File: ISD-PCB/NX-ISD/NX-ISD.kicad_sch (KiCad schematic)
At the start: 1 part

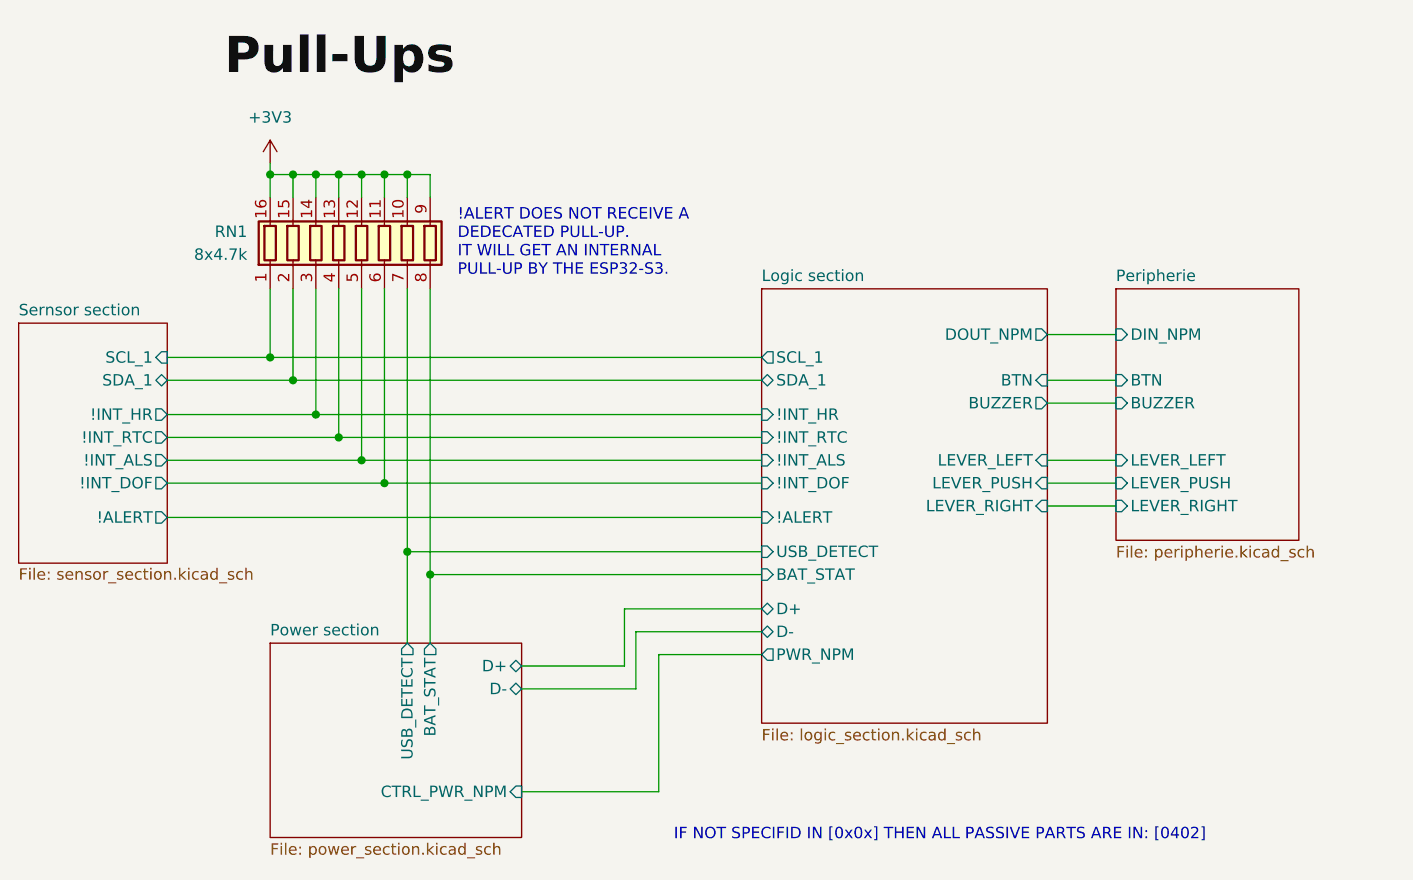
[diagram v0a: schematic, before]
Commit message: Fixed: polarity of NPM Pmos
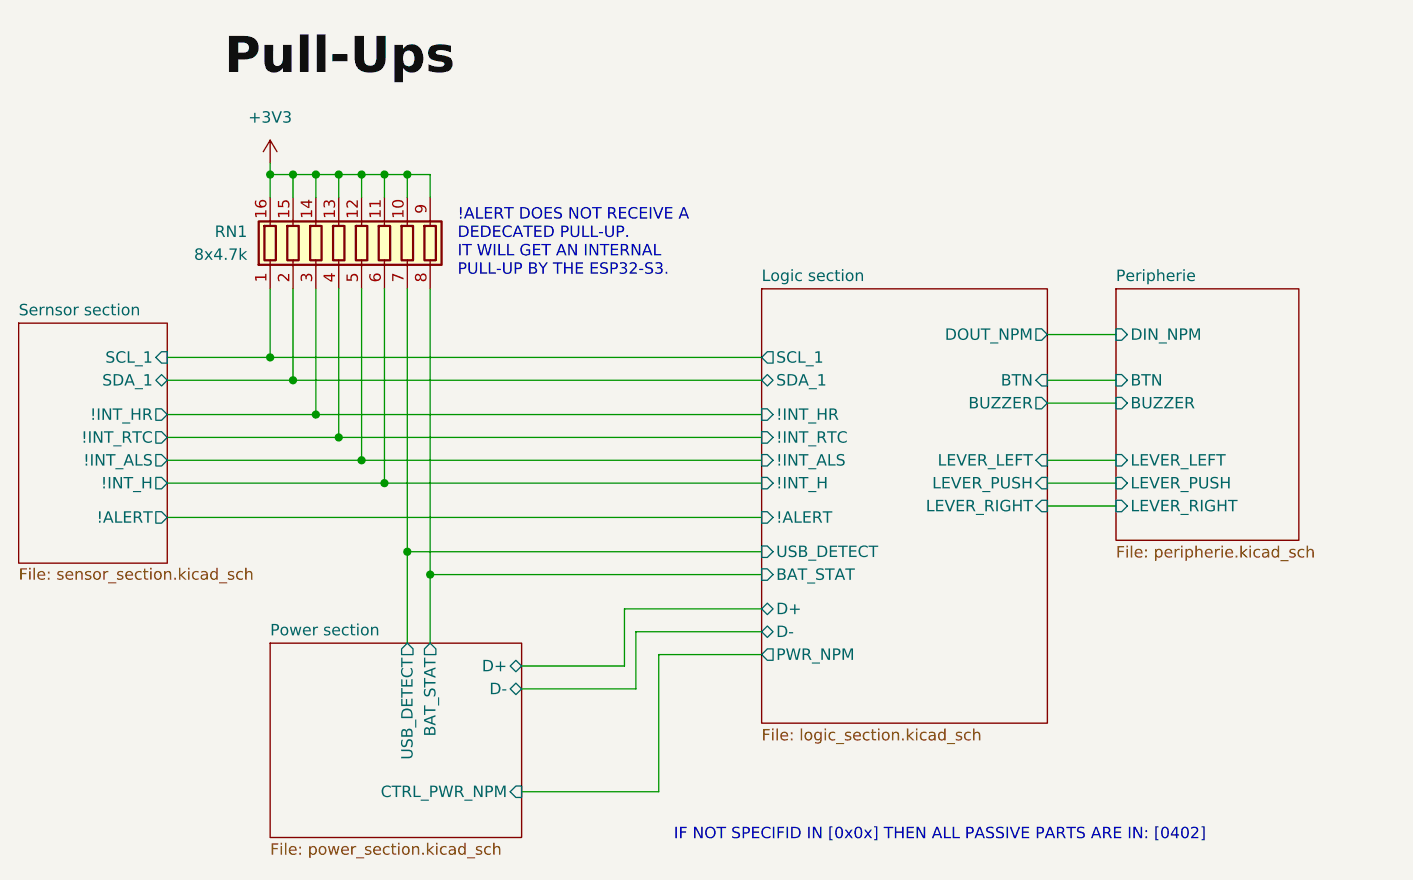
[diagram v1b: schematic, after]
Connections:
- net Logic section/!INT_DOF renamed Logic section/!INT_H
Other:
- sheet Logic section ports: added !INT_H; removed !INT_DOF
- sheet Sernsor section ports: added !INT_H; removed !INT_DOF
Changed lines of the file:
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@@
 			)
 		)
-		(pin "!INT_DOF" input
+		(pin "!INT_H" input
 			(at 104.14 67.31 180)
 			(effects
@@
 			)
 		)
-		(pin "!INT_DOF" output
+		(pin "!INT_H" output
 			(at 38.1 67.31 0)
 			(effects

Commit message: updated labels
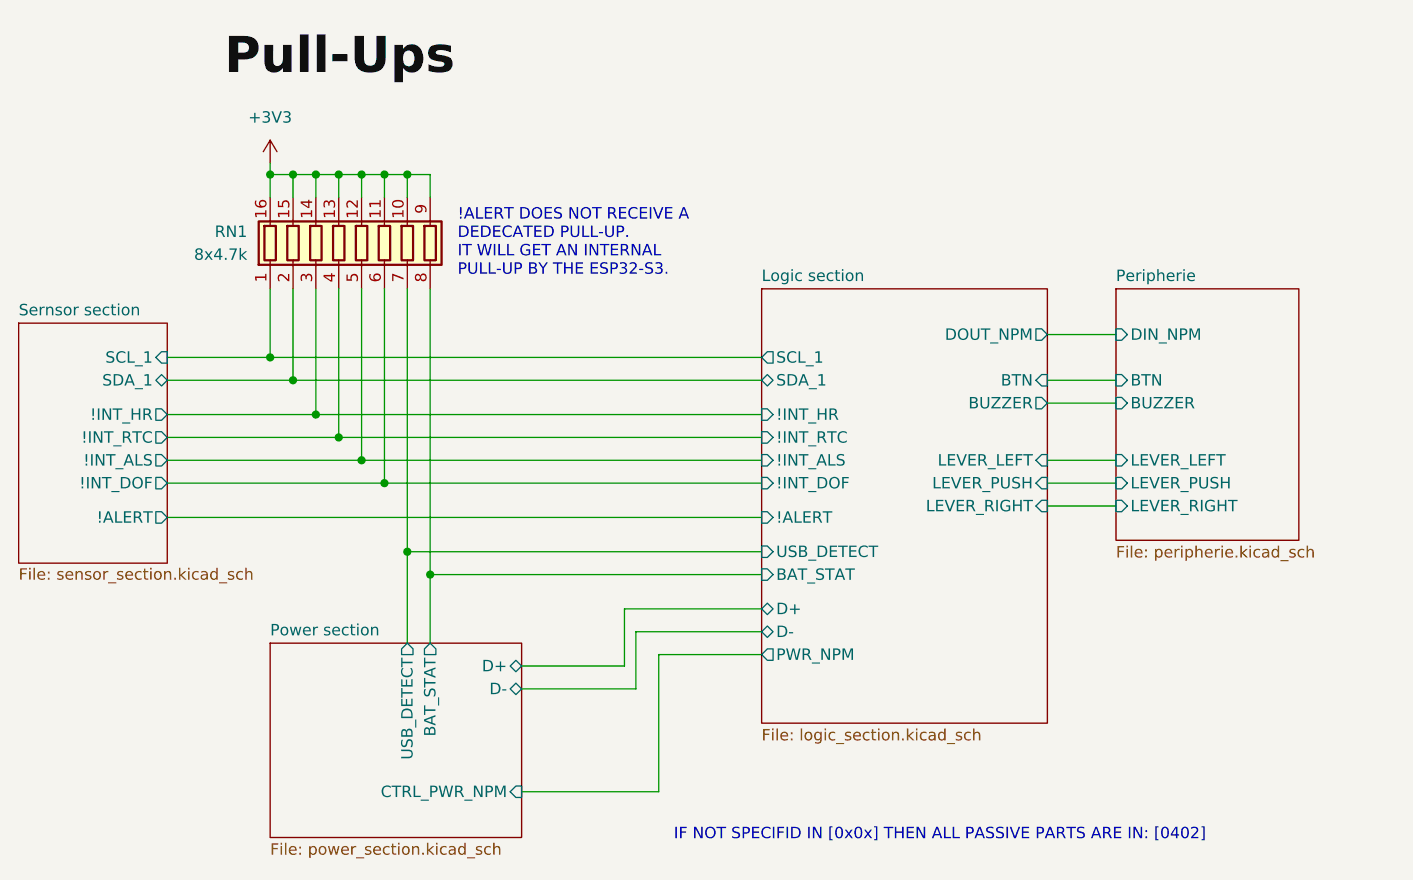
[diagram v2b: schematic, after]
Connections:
- net Logic section/!INT_H renamed Logic section/!INT_DOF
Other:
- sheet Logic section ports: added !INT_DOF; removed !INT_H
- sheet Sernsor section ports: added !INT_DOF; removed !INT_H
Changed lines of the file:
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@@
 			)
 		)
-		(pin "!INT_H" input
+		(pin "!INT_DOF" input
 			(at 104.14 67.31 180)
 			(effects
@@
 			)
 		)
-		(pin "!INT_H" output
+		(pin "!INT_DOF" output
 			(at 38.1 67.31 0)
 			(effects
